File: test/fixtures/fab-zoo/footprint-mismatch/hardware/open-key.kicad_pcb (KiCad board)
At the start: 2 copper layers, 40 x 30 mm, 3 parts, among them U1 ESP32-S3-MINI

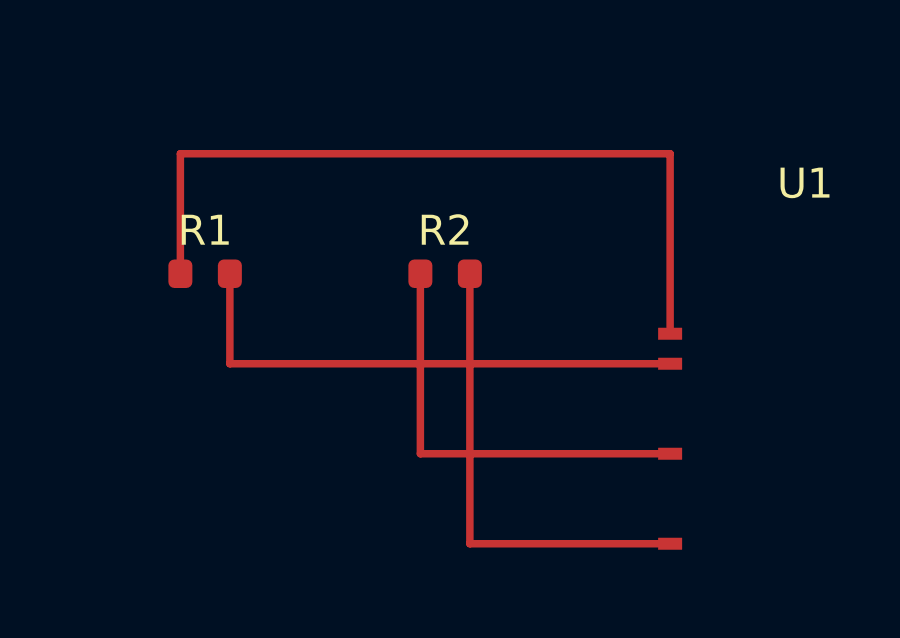
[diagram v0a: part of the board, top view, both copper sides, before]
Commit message: test(fab): fix crossing tracks in _base and generate real kicad-cli DRC reports (#14)
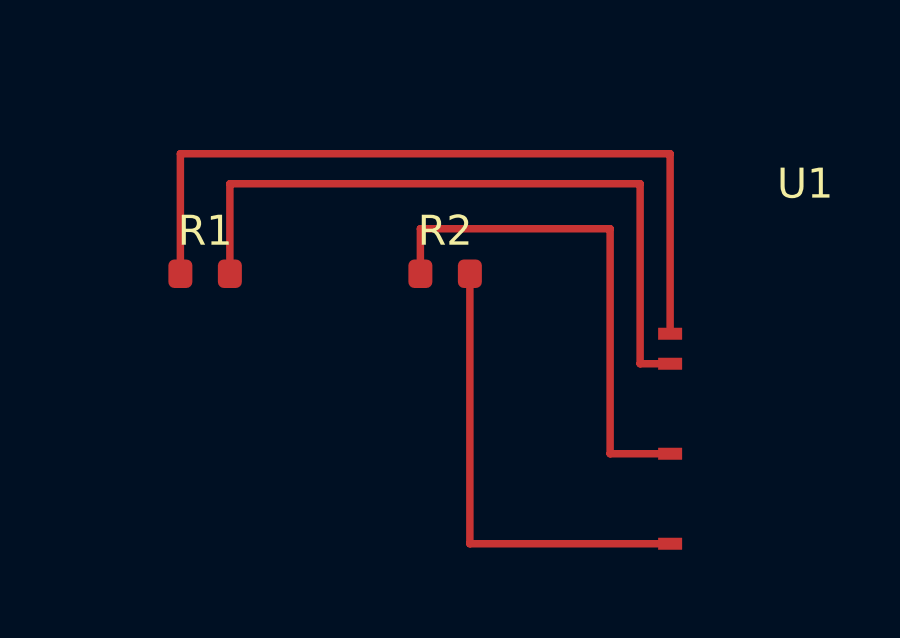
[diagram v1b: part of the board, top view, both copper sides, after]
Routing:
- net EN: track 17.7 -> 23.7 mm
- net KEY_DAH: track 14.3 -> 17.3 mm
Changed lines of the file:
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@@
   (segment (start 107.175 106) (end 123.5 106) (width 0.25) (layer "F.Cu") (net 1))
   (segment (start 123.5 106) (end 123.5 112) (width 0.25) (layer "F.Cu") (net 1))
-  (segment (start 108.825 110) (end 108.825 113) (width 0.25) (layer "F.Cu") (net 2))
-  (segment (start 108.825 113) (end 123.5 113) (width 0.25) (layer "F.Cu") (net 2))
+  (segment (start 108.825 110) (end 108.825 107) (width 0.25) (layer "F.Cu") (net 2))
+  (segment (start 108.825 107) (end 122.5 107) (width 0.25) (layer "F.Cu") (net 2))
+  (segment (start 122.5 107) (end 122.5 113) (width 0.25) (layer "F.Cu") (net 2))
+  (segment (start 122.5 113) (end 123.5 113) (width 0.25) (layer "F.Cu") (net 2))
   (segment (start 116.825 110) (end 116.825 119) (width 0.25) (layer "F.Cu") (net 3))
   (segment (start 116.825 119) (end 123.5 119) (width 0.25) (layer "F.Cu") (net 3))
-  (segment (start 115.175 110) (end 115.175 116) (width 0.25) (layer "F.Cu") (net 4))
-  (segment (start 115.175 116) (end 123.5 116) (width 0.25) (layer "F.Cu") (net 4))
+  (segment (start 115.175 110) (end 115.175 108.5) (width 0.25) (layer "F.Cu") (net 4))
+  (segment (start 115.175 108.5) (end 121.5 108.5) (width 0.25) (layer "F.Cu") (net 4))
+  (segment (start 121.5 108.5) (end 121.5 116) (width 0.25) (layer "F.Cu") (net 4))
+  (segment (start 121.5 116) (end 123.5 116) (width 0.25) (layer "F.Cu") (net 4))
 )
